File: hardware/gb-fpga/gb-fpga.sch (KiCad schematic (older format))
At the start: 4 parts

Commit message: Assign footprint and place fpga on board
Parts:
- U1: renamed from U?; footprint (none) -> Package_BGA:Xilinx_FTGB196
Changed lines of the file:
@@
 $EndDescr
 $Comp
-L xilinx7:xc7s25ftgb196 U?
+L xilinx7:xc7s25ftgb196 U1
 U 1 1 60CEDD39
 P 1950 1850
-F 0 "U?" H 2881 853 60  0000 L CNN
+F 0 "U1" H 2881 853 60  0000 L CNN
 F 1 "xc7s25ftgb196" H 2881 747 60  0000 L CNN
-F 2 "" H 2150 1900 60  0001 L CNN
+F 2 "Package_BGA:Xilinx_FTGB196" H 2150 1900 60  0001 L CNN
 F 3 "" H 2150 1700 60  0001 L CNN
 F 4 "xc7s25ftgb196" H 2150 1600 60  0001 L CNN "desc"
@@
 $EndComp
 $Comp
-L xilinx7:xc7s25ftgb196 U?
+L xilinx7:xc7s25ftgb196 U1
 U 2 1 60CF46E4
 P 4000 1750
-F 0 "U?" H 5731 -697 60  0000 L CNN
+F 0 "U1" H 5731 -697 60  0000 L CNN
 F 1 "xc7s25ftgb196" H 5731 -803 60  0000 L CNN
-F 2 "" H 4200 1800 60  0001 L CNN
+F 2 "Package_BGA:Xilinx_FTGB196" H 4200 1800 60  0001 L CNN
 F 3 "" H 4200 1600 60  0001 L CNN
 F 4 "xc7s25ftgb196" H 4200 1500 60  0001 L CNN "desc"
@@
 $EndComp
 $Comp
-L xilinx7:xc7s25ftgb196 U?
+L xilinx7:xc7s25ftgb196 U1
 U 3 1 60CF7DA5
 P 6700 1200
-F 0 "U?" H 7931 -1247 60  0000 L CNN
+F 0 "U1" H 7931 -1247 60  0000 L CNN
 F 1 "xc7s25ftgb196" H 7931 -1353 60  0000 L CNN
-F 2 "" H 6900 1250 60  0001 L CNN
+F 2 "Package_BGA:Xilinx_FTGB196" H 6900 1250 60  0001 L CNN
 F 3 "" H 6900 1050 60  0001 L CNN
 F 4 "xc7s25ftgb196" H 6900 950 60  0001 L CNN "desc"
@@
 $EndComp
 $Comp
-L xilinx7:xc7s25ftgb196 U?
+L xilinx7:xc7s25ftgb196 U1
 U 4 1 60CFF16A
 P 9050 2300
-F 0 "U?" H 9881 2203 60  0000 L CNN
+F 0 "U1" H 9881 2203 60  0000 L CNN
 F 1 "xc7s25ftgb196" H 9881 2097 60  0000 L CNN
-F 2 "" H 9250 2350 60  0001 L CNN
+F 2 "Package_BGA:Xilinx_FTGB196" H 9250 2350 60  0001 L CNN
 F 3 "" H 9250 2150 60  0001 L CNN
 F 4 "xc7s25ftgb196" H 9250 2050 60  0001 L CNN "desc"

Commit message: Add hierarchical sheets
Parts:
- removed U1: xc7s25ftgb196, Package_BGA:Xilinx_FTGB196, symbol xilinx7:xc7s25ftgb196
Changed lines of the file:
@@
 $Descr A4 11693 8268
 encoding utf-8
-Sheet 1 1
-Title ""
+Sheet 1 4
+Title "GB FPGA"
 Date ""
 Rev ""
@@
 Comment4 ""
 $EndDescr
-$Comp
-L xilinx7:xc7s25ftgb196 U1
-U 1 1 60CEDD39
-P 1950 1850
-F 0 "U1" H 2881 853 60  0000 L CNN
-F 1 "xc7s25ftgb196" H 2881 747 60  0000 L CNN
-F 2 "Package_BGA:Xilinx_FTGB196" H 2150 1900 60  0001 L CNN
-F 3 "" H 2150 1700 60  0001 L CNN
-F 4 "xc7s25ftgb196" H 2150 1600 60  0001 L CNN "desc"
-	1    1950 1850
-	1    0    0    -1
-$EndComp
-$Comp
-L xilinx7:xc7s25ftgb196 U1
-U 2 1 60CF46E4
-P 4000 1750
-F 0 "U1" H 5731 -697 60  0000 L CNN
-F 1 "xc7s25ftgb196" H 5731 -803 60  0000 L CNN
-F 2 "Package_BGA:Xilinx_FTGB196" H 4200 1800 60  0001 L CNN
-F 3 "" H 4200 1600 60  0001 L CNN
-F 4 "xc7s25ftgb196" H 4200 1500 60  0001 L CNN "desc"
-	2    4000 1750
-	1    0    0    -1
-$EndComp
-$Comp
-L xilinx7:xc7s25ftgb196 U1
-U 3 1 60CF7DA5
-P 6700 1200
-F 0 "U1" H 7931 -1247 60  0000 L CNN
-F 1 "xc7s25ftgb196" H 7931 -1353 60  0000 L CNN
-F 2 "Package_BGA:Xilinx_FTGB196" H 6900 1250 60  0001 L CNN
-F 3 "" H 6900 1050 60  0001 L CNN
-F 4 "xc7s25ftgb196" H 6900 950 60  0001 L CNN "desc"
-	3    6700 1200
-	1    0    0    -1
-$EndComp
-$Comp
-L xilinx7:xc7s25ftgb196 U1
-U 4 1 60CFF16A
-P 9050 2300
-F 0 "U1" H 9881 2203 60  0000 L CNN
-F 1 "xc7s25ftgb196" H 9881 2097 60  0000 L CNN
-F 2 "Package_BGA:Xilinx_FTGB196" H 9250 2350 60  0001 L CNN
-F 3 "" H 9250 2150 60  0001 L CNN
-F 4 "xc7s25ftgb196" H 9250 2050 60  0001 L CNN "desc"
-	4    9050 2300
-	1    0    0    -1
-$EndComp
+$Sheet
+S 1750 2250 500  150
+U 60D2592A
+F0 "Configuration" 50
+F1 "configuration.sch" 50
+$EndSheet
+$Sheet
+S 1750 1700 500  150
+U 60D22871
+F0 "Power" 50
+F1 "power.sch" 50
+$EndSheet
+$Sheet
+S 1750 2800 500  150
+U 60D200EC
+F0 "Banks" 50
+F1 "banks.sch" 50
+$EndSheet
 $EndSCHEMATC

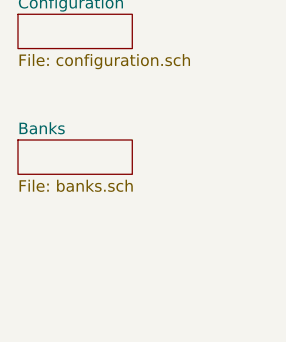
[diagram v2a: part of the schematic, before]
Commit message: Add usb parts
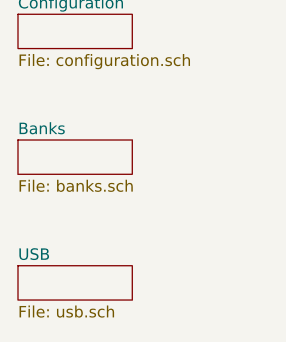
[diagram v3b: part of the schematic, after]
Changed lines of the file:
@@
 $Descr A4 11693 8268
 encoding utf-8
-Sheet 1 4
+Sheet 1 5
 Title "GB FPGA"
 Date ""
@@
 F1 "banks.sch" 50
 $EndSheet
+$Sheet
+S 1750 3350 500  150
+U 60D2FD9B
+F0 "USB" 50
+F1 "usb.sch" 50
+$EndSheet
 $EndSCHEMATC

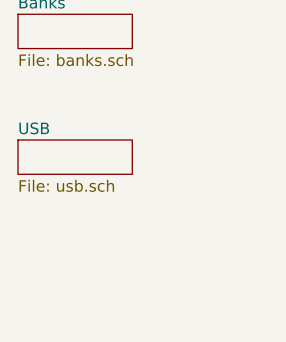
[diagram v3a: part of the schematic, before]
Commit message: Add and place cartridge footprint and place usb connector
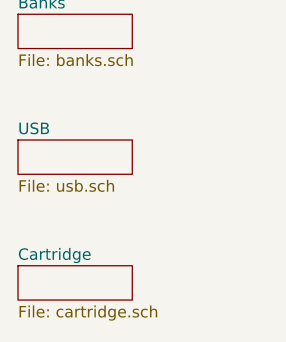
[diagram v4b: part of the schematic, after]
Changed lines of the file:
@@
 $Descr A4 11693 8268
 encoding utf-8
-Sheet 1 5
+Sheet 1 6
 Title "GB FPGA"
 Date ""
@@
 F1 "usb.sch" 50
 $EndSheet
+$Sheet
+S 1750 3900 500  150
+U 60D49E96
+F0 "Cartridge" 50
+F1 "cartridge.sch" 50
+$EndSheet
 $EndSCHEMATC

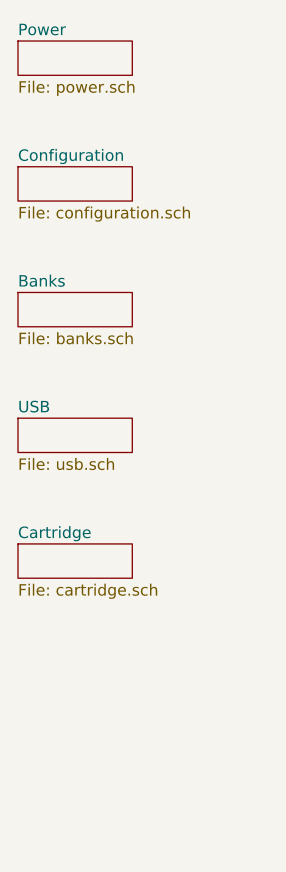
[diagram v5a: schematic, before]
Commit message: Add LTC3555
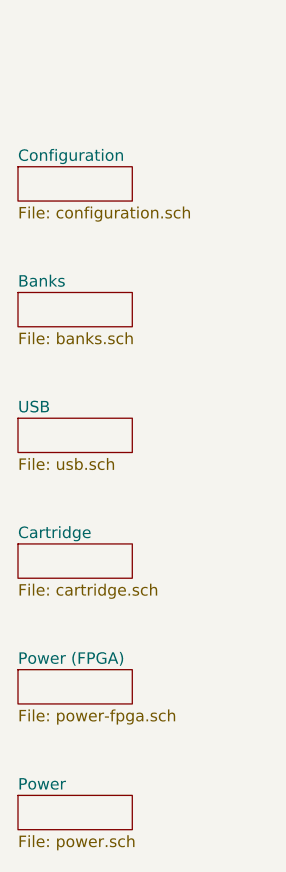
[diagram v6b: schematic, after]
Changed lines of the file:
@@
 $Descr A4 11693 8268
 encoding utf-8
-Sheet 1 6
+Sheet 1 7
 Title "GB FPGA"
 Date ""
@@
 $EndSheet
 $Sheet
-S 1750 1700 500  150
+S 1750 4450 500  150
 U 60D22871
+F0 "Power (FPGA)" 50
+F1 "power-fpga.sch" 50
+$EndSheet
+$Sheet
+S 1750 5000 500  150
+U 60D77322
 F0 "Power" 50
 F1 "power.sch" 50

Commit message: Add board connector
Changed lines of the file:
@@
 $Descr A4 11693 8268
 encoding utf-8
-Sheet 1 7
+Sheet 1 8
 Title "GB FPGA"
 Date ""
@@
 F1 "power.sch" 50
 $EndSheet
+$Sheet
+S 1750 5550 500  150
+U 60DDCCEF
+F0 "Board Connector" 50
+F1 "board-connector.sch" 50
+$EndSheet
 $EndSCHEMATC

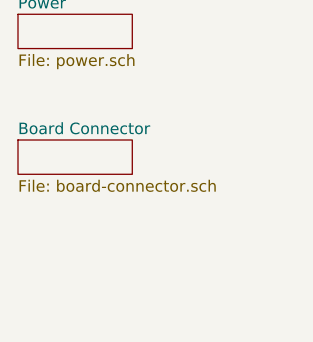
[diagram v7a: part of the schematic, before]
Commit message: Add test points and update gerber for pcb way
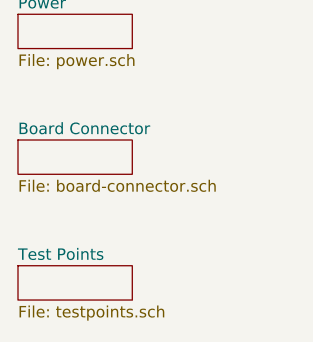
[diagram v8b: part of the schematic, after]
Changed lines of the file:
@@
 $Descr A4 11693 8268
 encoding utf-8
-Sheet 1 8
+Sheet 1 9
 Title "GB FPGA"
 Date ""
@@
 F1 "board-connector.sch" 50
 $EndSheet
+$Sheet
+S 1750 6100 500  150
+U 60E56A33
+F0 "Test Points" 50
+F1 "testpoints.sch" 50
+$EndSheet
 $EndSCHEMATC
